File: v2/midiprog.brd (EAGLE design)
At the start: 99.1 x 78.7 mm, 56 parts, among them IC1 PIC18F4550_40, IC2 TPIC6B596N, IC4 TPIC6B596N, Q2 2N2222A, Q3 2N2222A, Q4 2N2222A, Q5 8MHz

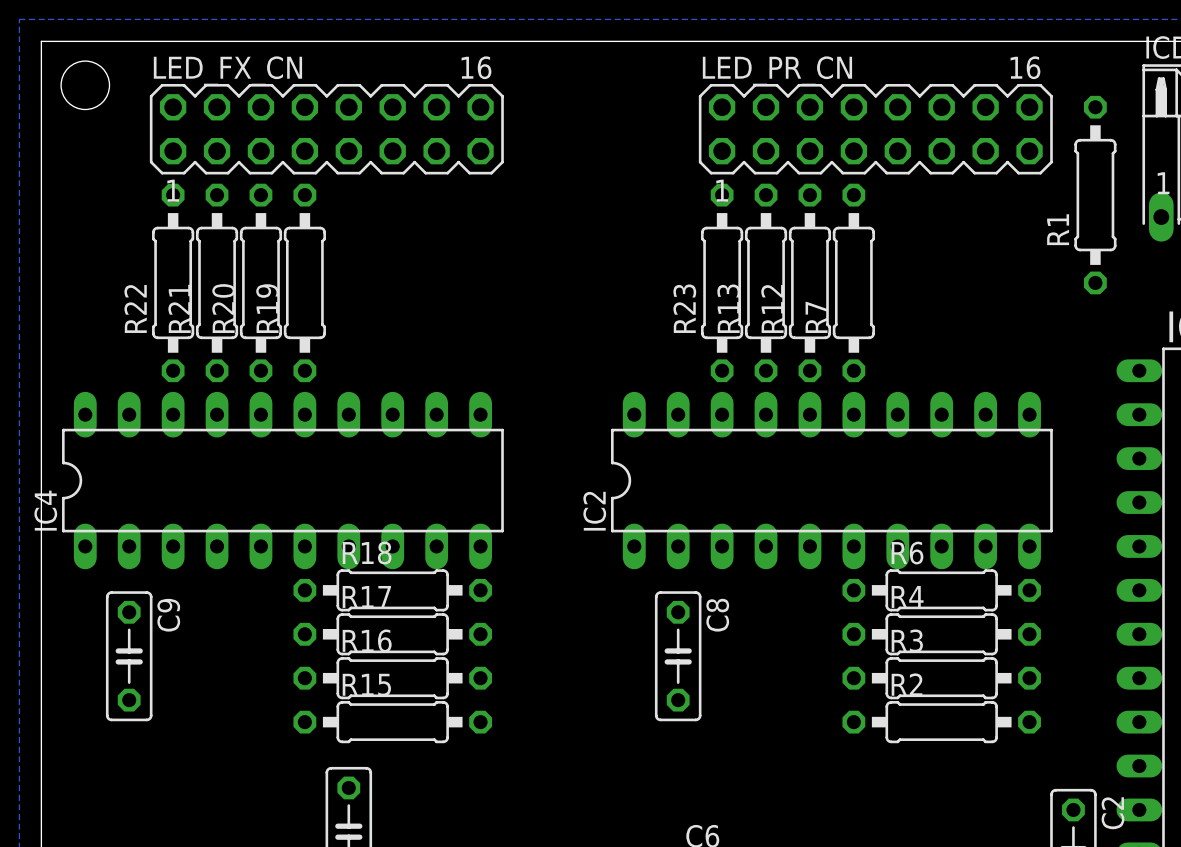
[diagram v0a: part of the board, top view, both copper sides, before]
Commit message: Much tighter LED routing now.
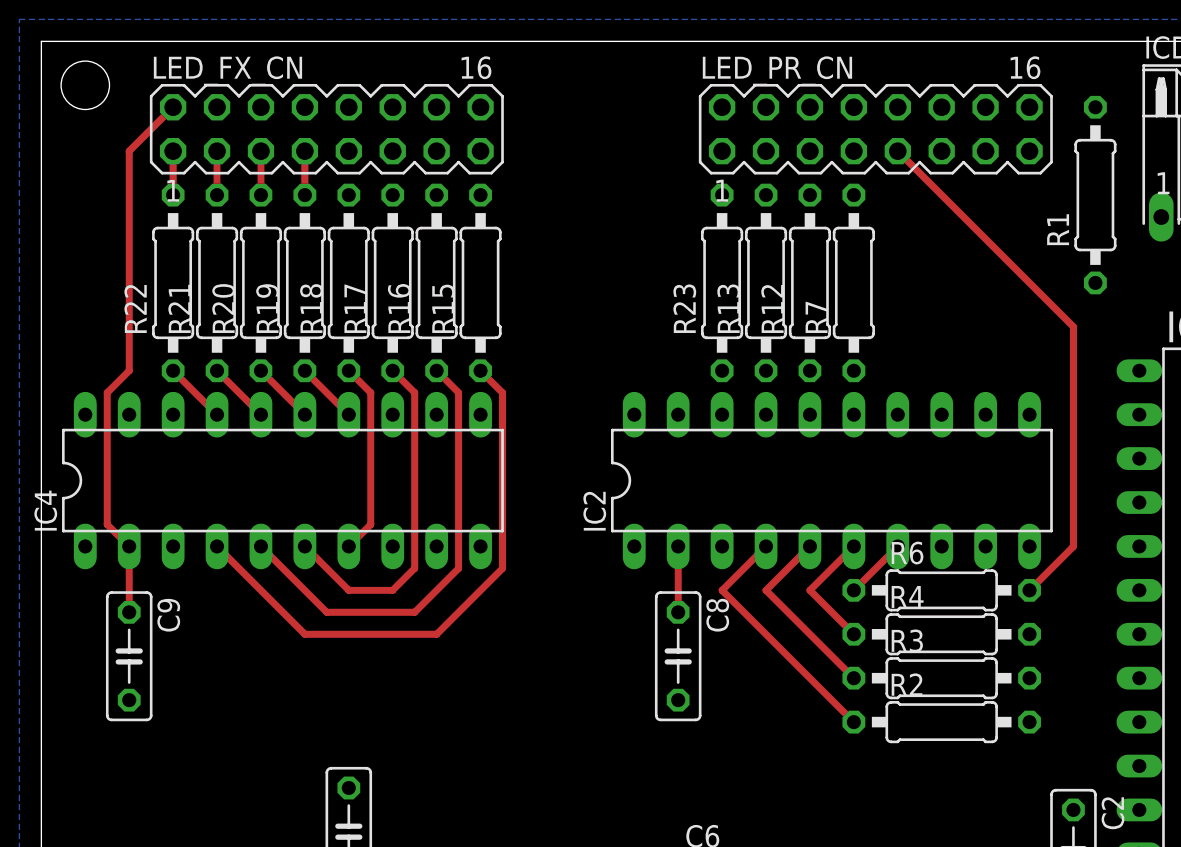
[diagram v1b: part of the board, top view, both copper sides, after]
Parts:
- moved R15 25.9 mm to (25.4, 64.8), turned to 90 degrees
- moved R16 23.0 mm to (22.9, 64.8), turned to 90 degrees
- moved R17 20.3 mm to (20.3, 64.8), turned to 90 degrees
- moved R18 18.0 mm to (17.8, 64.8), turned to 90 degrees
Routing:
- net VDD: track 0.00 -> 35.1 mm
- net N$19: track 0.00 -> 32.1 mm
- net N$28: track 0.00 -> 30.7 mm
- net N$20: track 0.00 -> 26.0 mm
- net N$21: track 0.00 -> 19.9 mm
- net N$38: track 0.00 -> 14.4 mm
- net N$22: track 0.00 -> 11.2 mm
- net N$39: track 0.00 -> 10.8 mm
- net N$40: track 0.00 -> 7.18 mm
- net N$29: track 0.00 -> 3.59 mm
- net N$25: track 0.00 -> 3.59 mm
- net N$23: track 0.00 -> 3.59 mm
- net N$41: track 0.00 -> 3.59 mm
- net N$26: track 0.00 -> 3.59 mm
- net N$15: track 0.00 -> 2.54 mm
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
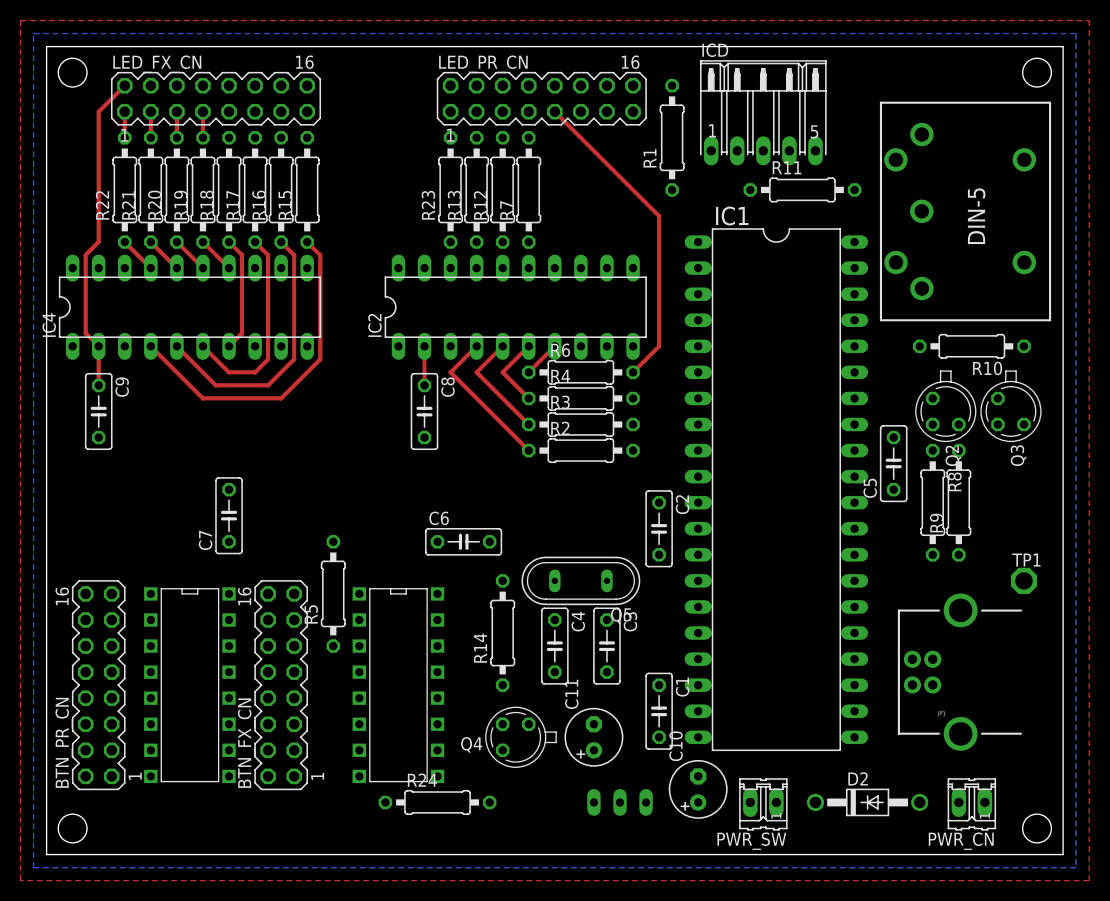
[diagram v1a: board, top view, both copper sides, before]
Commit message: Got LEDs manually routed very tightly. Working on buttons.
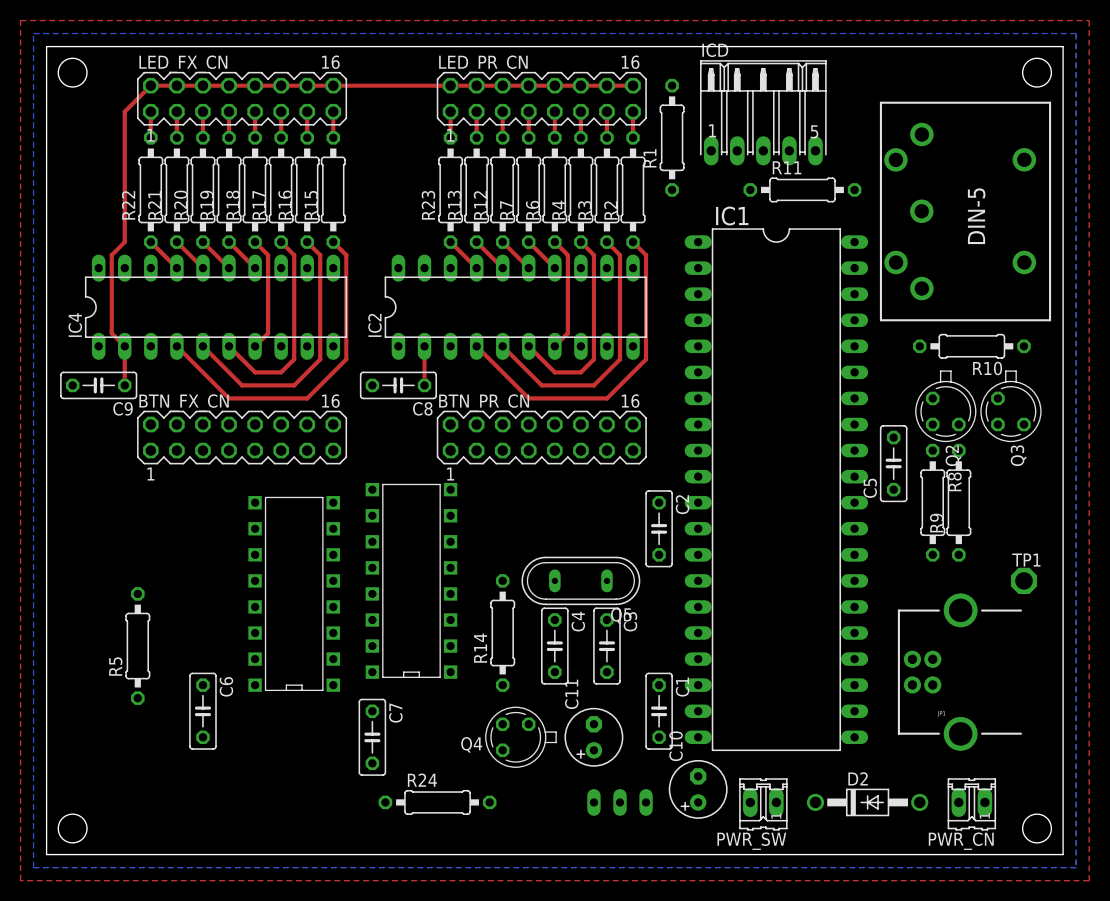
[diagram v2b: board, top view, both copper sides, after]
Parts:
- moved BTN_PR_CN 49.5 mm to (48.3, 40.6), turned to 0 degrees
- moved C6 30.3 mm to (15.2, 14.0), turned to 270 degrees
- moved R2 25.9 mm to (57.1, 64.8), turned to 90 degrees
- moved C7 25.7 mm to (31.8, 11.4), turned to 270 degrees
- moved BTN_FX_CN 24.4 mm to (19.1, 40.6), turned to 0 degrees
- moved R3 23.0 mm to (54.6, 64.8), turned to 90 degrees
- moved U$2 21.1 mm to (20.3, 26.7), turned to 90 degrees
- moved R4 20.3 mm to (52.1, 64.8), turned to 90 degrees
- moved R5 19.7 mm to (8.89, 20.3)
- moved U$1 18.9 mm to (31.8, 27.9), turned to 90 degrees
- moved R6 18.0 mm to (49.5, 64.8), turned to 90 degrees
- moved C8 3.59 mm to (34.3, 45.7), turned to 180 degrees
- moved R15 2.54 mm to (27.9, 64.8)
- moved IC4 2.54 mm to (16.5, 53.3)
- moved R19 2.54 mm to (17.8, 64.8)
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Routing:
- net VDD: track 35.1 -> 82.1 mm
- net N$28: track 30.7 -> 2.54 mm
- net N$38: track 14.4 -> 32.1 mm
- net N$39: track 10.8 -> 26.0 mm
- net N$40: track 7.18 -> 19.9 mm
- net N$41: track 3.59 -> 11.2 mm
- net N$44: track 0.00 -> 3.59 mm
- net N$45: track 0.00 -> 3.59 mm
- net N$43: track 0.00 -> 3.59 mm
- net N$42: track 0.00 -> 3.59 mm
- net N$6: track 0.00 -> 2.54 mm
- net N$37: track 0.00 -> 2.54 mm
- net N$36: track 0.00 -> 2.54 mm
- net N$32: track 0.00 -> 2.54 mm
- net N$30: track 0.00 -> 2.54 mm
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
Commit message: Good layout on buttons and LEDs.
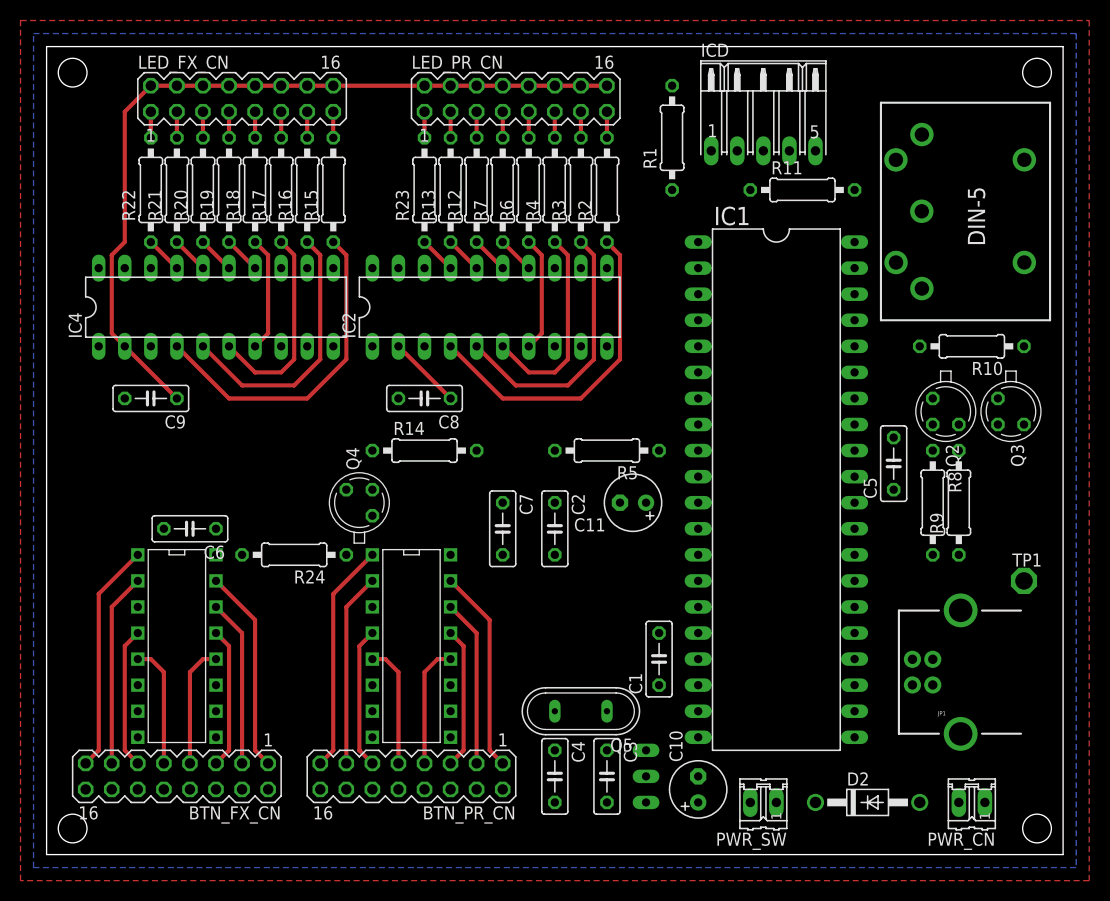
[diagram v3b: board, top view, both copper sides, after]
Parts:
- moved R5 49.5 mm to (54.6, 39.4), turned to 180 degrees
- moved BTN_PR_CN 35.4 mm to (35.6, 7.62), turned to 180 degrees
- moved BTN_FX_CN 33.6 mm to (12.7, 7.62), turned to 180 degrees
- moved R24 27.9 mm to (24.1, 29.2), turned to 180 degrees
- moved Q4 27.5 mm to (30.5, 34.3), turned to 90 degrees
- moved C7 24.0 mm to (44.5, 31.8)
- moved C11 23.2 mm to (57.1, 34.3), turned to 180 degrees
- moved R14 19.3 mm to (36.8, 39.4), turned to 0 degrees
- moved C6 17.8 mm to (14.0, 31.8), turned to 180 degrees
- moved Q5 12.7 mm to (52.1, 14.0)
- moved C3 12.7 mm to (54.6, 7.62)
- moved C4 12.7 mm to (49.5, 7.62)
- moved U$1 11.7 mm to (39.4, 19.1), turned to 270 degrees
- moved C2 10.2 mm to (49.5, 31.8)
- moved U$2 8.52 mm to (16.5, 19.1), turned to 270 degrees
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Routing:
- net N$60: track 0.00 -> 22.4 mm
- net N$52: track 0.00 -> 22.4 mm
- net N$58: track 0.00 -> 19.9 mm
- net N$64: track 0.00 -> 19.9 mm
- net N$51: track 0.00 -> 18.8 mm
- net N$49: track 0.00 -> 18.8 mm
- net N$63: track 0.00 -> 16.3 mm
- net N$57: track 0.00 -> 16.3 mm
- net N$56: track 0.00 -> 13.8 mm
- net N$62: track 0.00 -> 13.8 mm
- net N$50: track 0.00 -> 13.8 mm
- net N$48: track 0.00 -> 13.8 mm
- net N$61: track 0.00 -> 12.0 mm
- net N$47: track 0.00 -> 12.0 mm
- net N$55: track 0.00 -> 12.0 mm
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
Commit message: Autorouted; meh.
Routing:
- net VDD: track 86.3 -> 300.4 mm
- net BTN_S2: track 0.00 -> 96.6 mm, vias 0 -> 1
- net BTN_IN: track 0.00 -> 95.7 mm
- net BTN_S3: track 0.00 -> 85.9 mm
- net BTN_S0: track 0.00 -> 71.1 mm, vias 0 -> 1
- net BTN_S1: track 0.00 -> 71.0 mm
- net SHIFTREG_RCK: track 0.00 -> 59.8 mm, vias 0 -> 2
- net N$54: track 0.00 -> 53.4 mm
- net SHIFTREG_SCL: track 0.00 -> 46.2 mm
- net N$31: track 0.00 -> 37.3 mm
- net SHIFTREG_D: track 0.00 -> 30.3 mm
- net OSC1: track 0.00 -> 25.6 mm
- net OSC2: track 0.00 -> 20.9 mm
- net N$16: track 0.00 -> 15.9 mm
- net USB_VCC: track 0.00 -> 14.4 mm
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
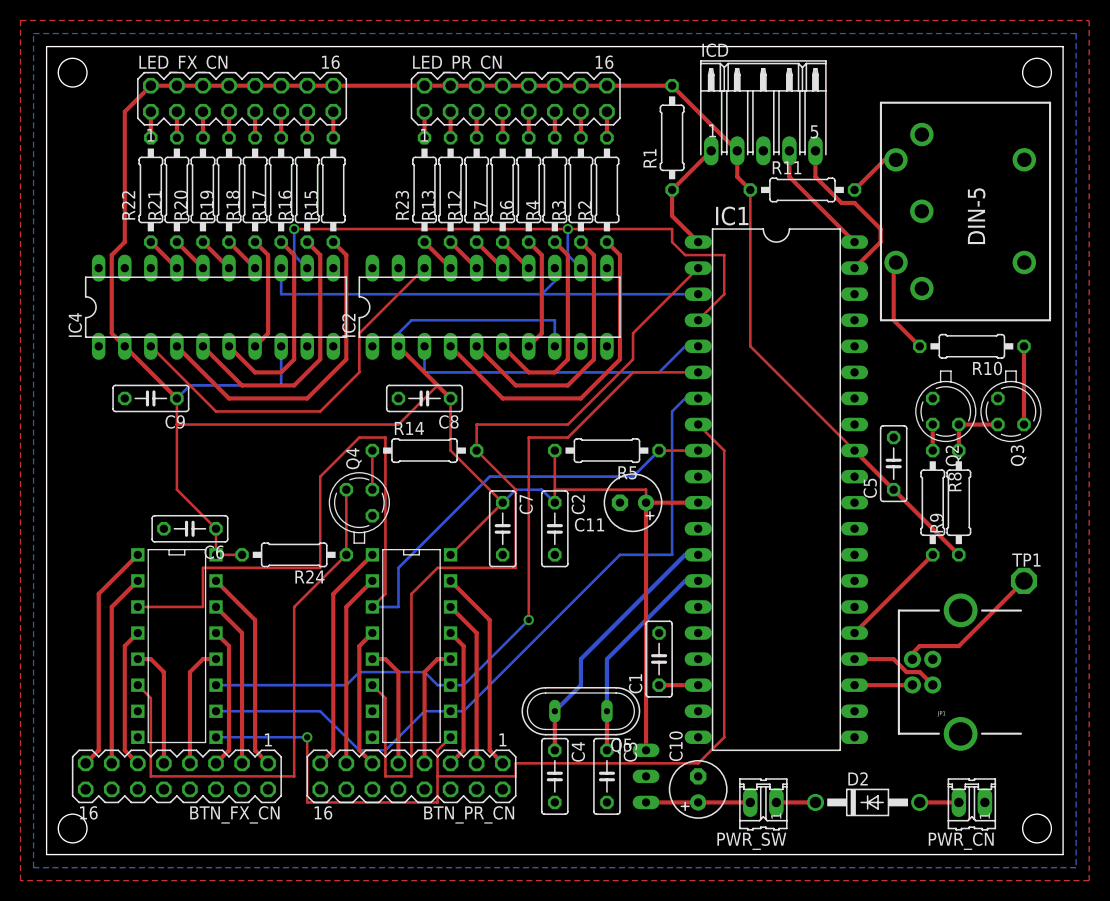
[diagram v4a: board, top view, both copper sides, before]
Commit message: Manually correcting more autorouter bloopers.
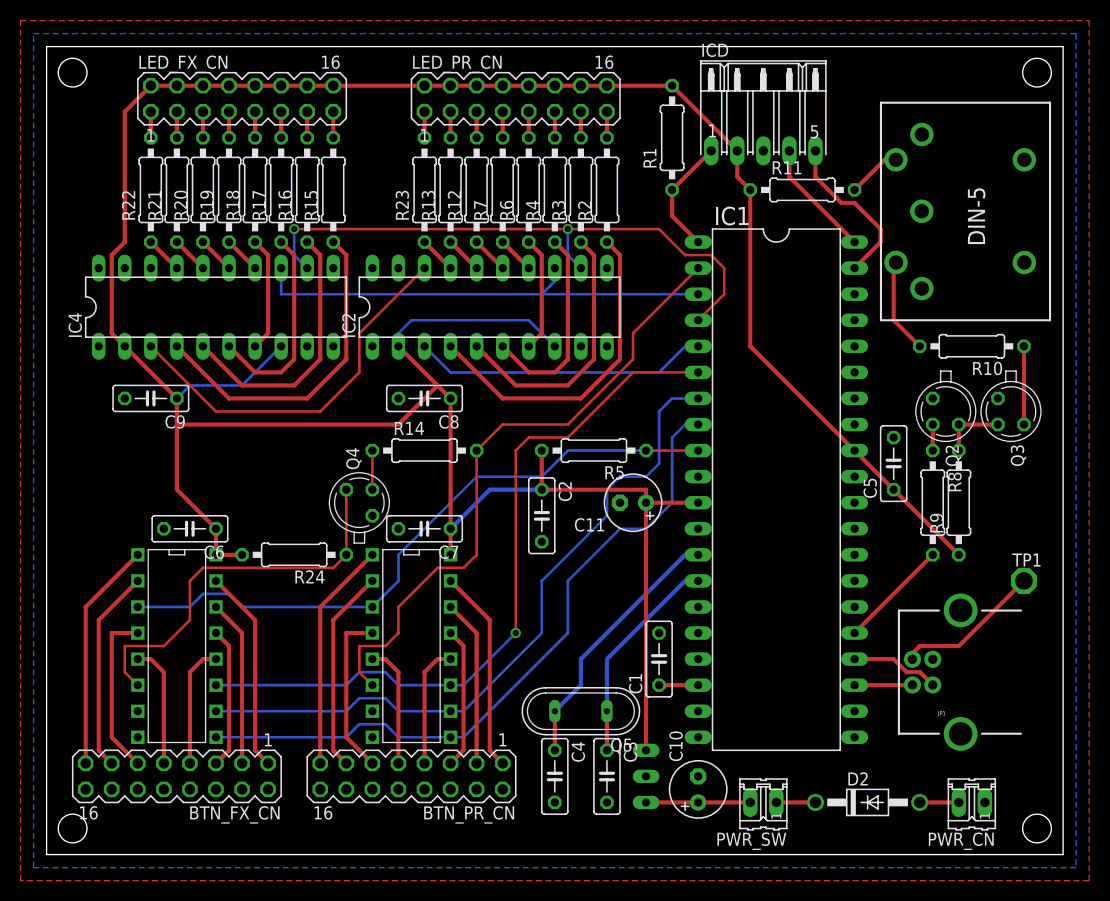
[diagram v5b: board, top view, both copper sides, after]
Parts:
- moved C7 7.62 mm to (36.8, 31.8), turned to 180 degrees
- moved C2 1.80 mm to (48.3, 33.0)
- moved R5 1.27 mm to (53.3, 39.4)
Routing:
- net BTN_IN: track 95.7 -> 63.5 mm
- net BTN_S2: track 96.6 -> 67.4 mm, vias 1 -> 0
- net BTN_S3: track 85.9 -> 61.5 mm
- net N$54: track 53.4 -> 38.2 mm
- net VDD: track 300.4 -> 296.8 mm
- net BTN_S1: track 71.0 -> 68.1 mm
- net N$48: track 13.8 -> 16.3 mm
- net N$50: track 13.8 -> 16.3 mm
- net SHIFTREG_RCK: track 59.8 -> 58.3 mm
- net SHIFTREG_D: track 30.3 -> 28.8 mm
- net N$51: track 18.8 -> 19.9 mm
- net N$49: track 18.8 -> 19.9 mm
